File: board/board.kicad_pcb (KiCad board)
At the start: 2 copper layers, 195 x 160 mm, 234 parts, among them J1 Conn_02x03_Odd_Even, J3 RPi_GPIO, SW1 SW_Push, SW2 SW_Push, SW3 SW_Push, SW4 SW_Push, U1 74HC238, U10 A3144, U11 A3144, U12 A3144, U13 A3144, U14 A3144, U15 A3144, U16 A3144, U17 A3144, U18 A3144, U19 A3144, U2 74LS151, U20 A3144, U21 A3144, U22 A3144, U23 A3144, U24 A3144, U25 A3144, U26 A3144, U27 A3144, U28 A3144, U29 A3144, U3 A3144, U30 A3144, U31 A3144, U32 A3144, U33 A3144, U34 A3144, U35 A3144, U36 A3144, U37 A3144, U38 A3144, U39 A3144, U4 A3144, U40 A3144, U41 A3144, U42 A3144, U43 A3144, U44 A3144, U45 A3144, U46 A3144, U47 A3144, U48 A3144, U49 A3144, U5 A3144, U50 A3144, U51 A3144, U52 A3144, U53 A3144, U54 A3144, U55 A3144, U56 A3144, U57 A3144, U58 A3144, U59 A3144, U6 A3144, U60 A3144, U61 A3144, U62 A3144, U63 A3144, U64 A3144, U65 A3144, U66 A3144, U7 A3144, U8 A3144, U9 A3144

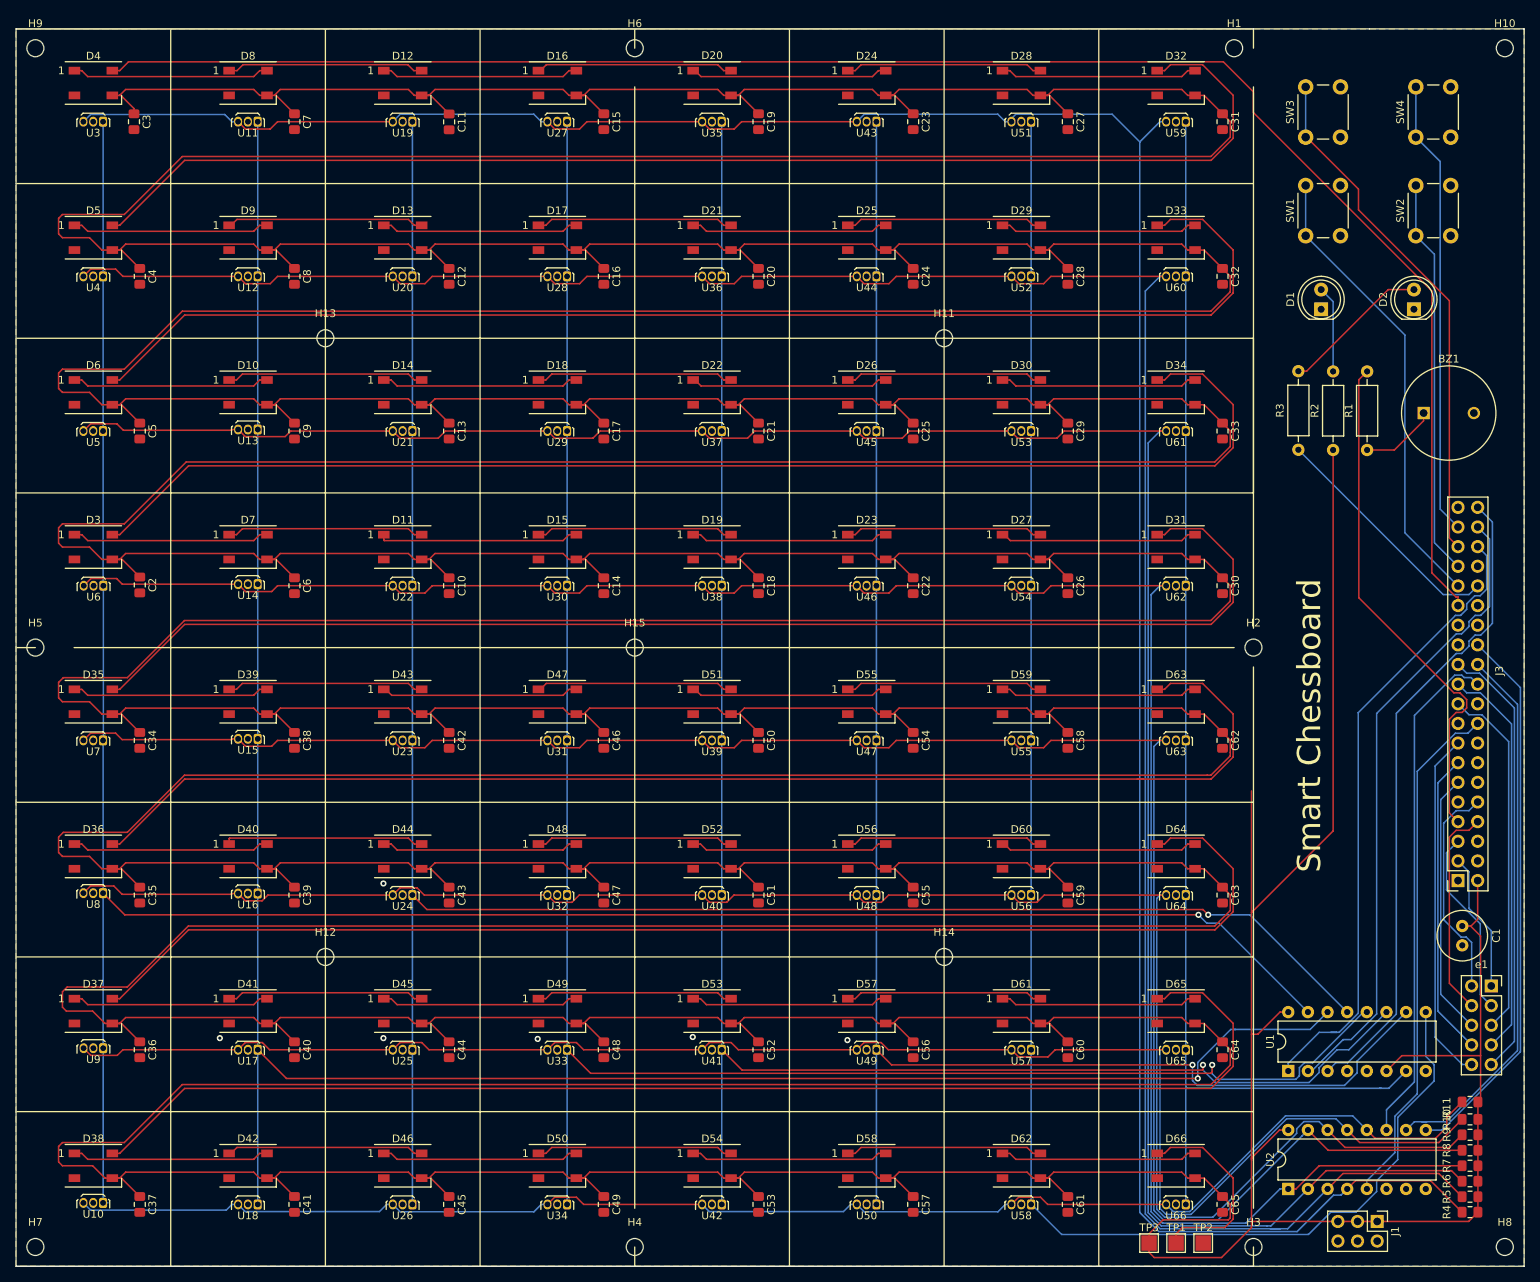
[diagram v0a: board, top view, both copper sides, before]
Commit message: Raspberry pi zero outline added
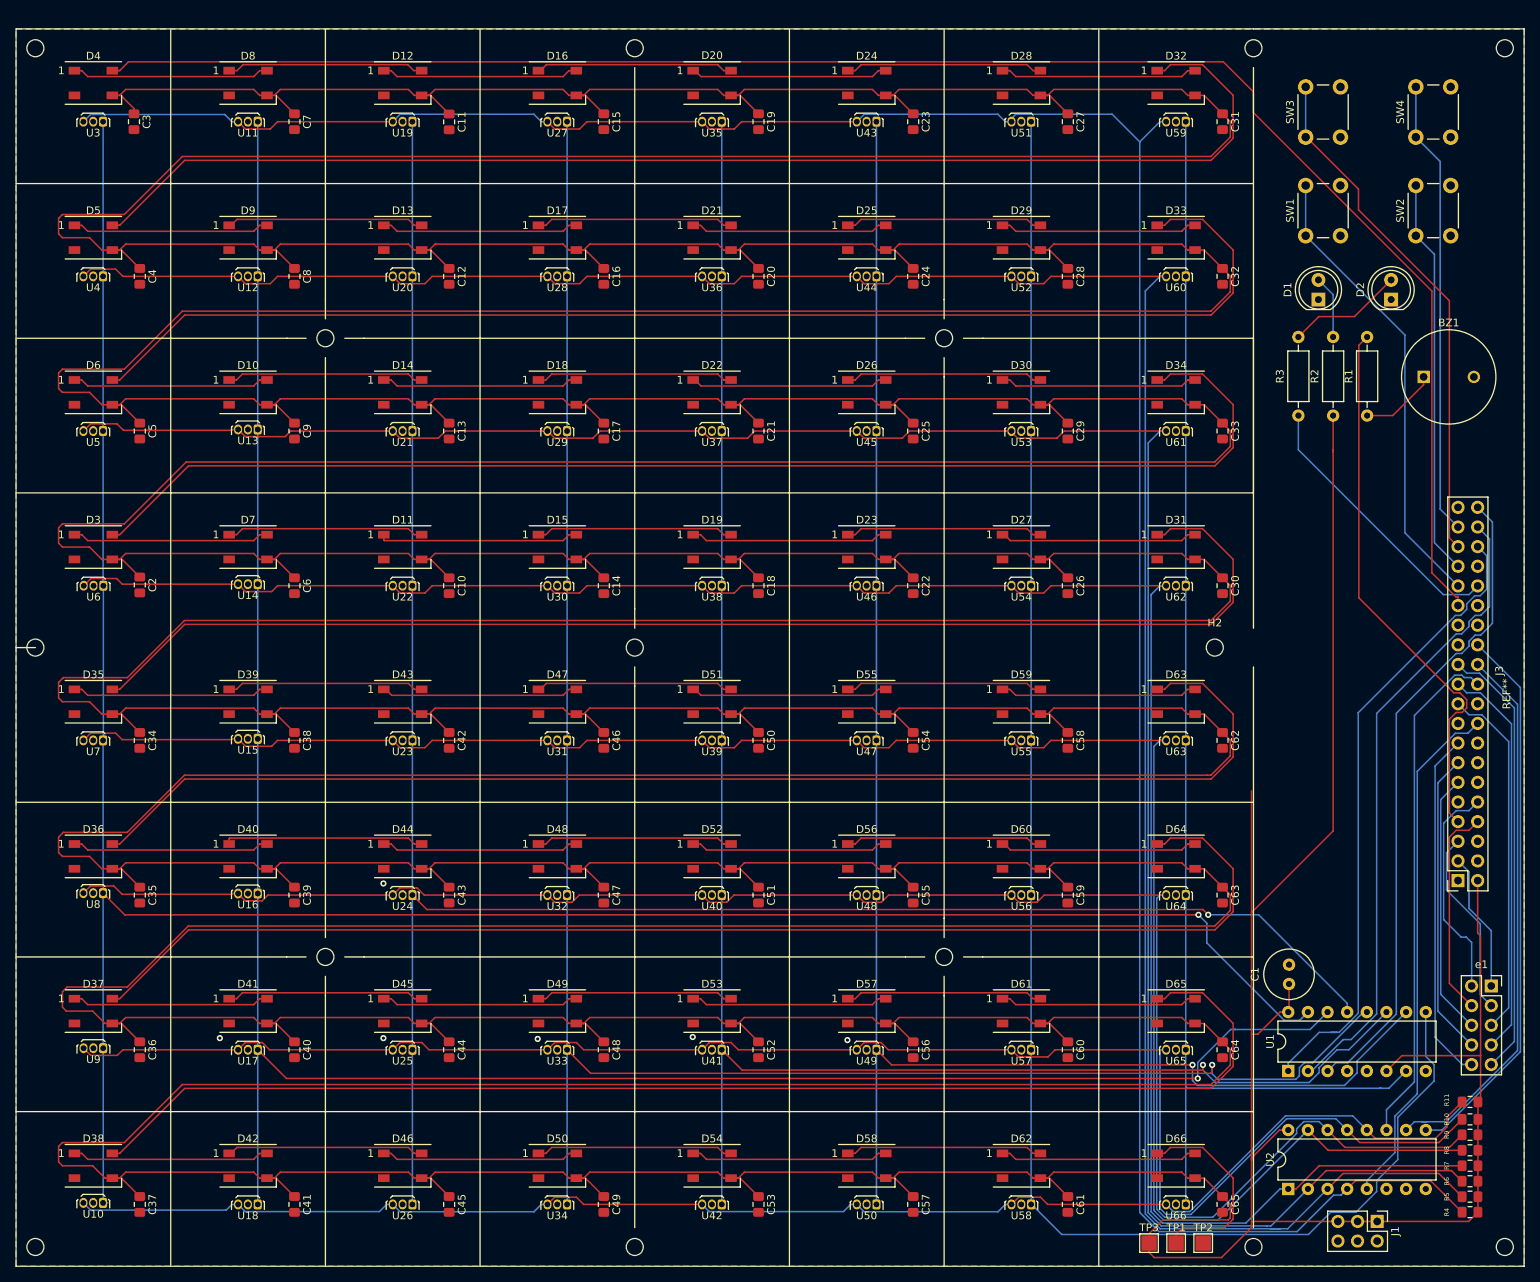
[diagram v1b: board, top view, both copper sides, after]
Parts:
- added REF**: rpi_zero_outline, board:rpi_zero_outline, F.Cu at (246.5, 160.1)
- moved C1 23.6 mm to (224.6, 173.5), turned to 90 degrees
- moved H2 5.00 mm to (215.0, 130.0)
- moved BZ1 4.67 mm to (242.0, 95.0)
- moved R1 4.45 mm to (234.7, 100.0)
- moved R2 4.45 mm to (230.3, 100.0)
- moved R3 4.42 mm to (225.8, 100.0)
- moved D2 3.20 mm to (237.8, 85.0)
- moved H1 2.50 mm to (220.0, 52.5)
- moved D1 1.30 mm to (228.4, 85.0)
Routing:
- net +5V: track 2879.4 -> 2885.9 mm
- net /BUZZER: track 66.7 -> 71.2 mm
- net /STAT_LED: track 31.4 -> 35.8 mm
- net Net-(D2-Pad2): track 19.3 -> 15.1 mm
- net Net-(D1-Pad2): track 11.2 -> 8.17 mm
- net D_0: track 302.6 -> 305.0 mm
- net D_2: track 267.1 -> 267.8 mm
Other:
- board text added: "Smart chessboard"
- board text removed: "Chessboard"
- board text removed: "Smart"
- board text removed: "Smart Chessboard"

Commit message: WS2812B test code added
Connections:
- J3 pad 1: (no net) -> Net-(J3-Pad1)
- J3 pad 12: (no net) -> LED_DATA
- J3 pad 14: (no net) -> Net-(J3-Pad14)
- J3 pad 16: (no net) -> Net-(J3-Pad16)
- J3 pad 17: (no net) -> Net-(J3-Pad17)
- J3 pad 20: (no net) -> Net-(J3-Pad20)
- J3 pad 25: (no net) -> Net-(J3-Pad25)
- J3 pad 27: (no net) -> Net-(J3-Pad27)
- J3 pad 28: (no net) -> Net-(J3-Pad28)
- J3 pad 29: LED_DATA -> Net-(J3-Pad29)
- J3 pad 30: (no net) -> Net-(J3-Pad30)
- J3 pad 34: (no net) -> Net-(J3-Pad34)
- J3 pad 4: (no net) -> Net-(J3-Pad4)
- J3 pad 6: (no net) -> Net-(J3-Pad6)
- J3 pad 9: (no net) -> Net-(J3-Pad9)
- U2 pad 6: (no net) -> Net-(U2-Pad6)
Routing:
- net LED_DATA: track 227.2 -> 254.5 mm
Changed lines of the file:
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@@
   (general
     (thickness 1.6)
-    (drawings 110)
-    (tracks 1612)
+    (drawings 114)
+    (tracks 1613)
     (zones 0)
     (modules 235)
-    (nets 110)
+    (nets 125)
   )
   (page A3)
@@
   (net 108 /AUX7)
   (net 109 /BTN4)
+  (net 110 "Net-(J3-Pad30)")
+  (net 111 "Net-(J3-Pad20)")
+  (net 112 "Net-(J3-Pad6)")
+  (net 113 "Net-(J3-Pad34)")
+  (net 114 "Net-(J3-Pad1)")
+  (net 115 "Net-(J3-Pad4)")
+  (net 116 "Net-(J3-Pad28)")
+  (net 117 "Net-(J3-Pad29)")
+  (net 118 "Net-(J3-Pad9)")
+  (net 119 "Net-(J3-Pad27)")
+  (net 120 "Net-(J3-Pad14)")
+  (net 121 "Net-(J3-Pad17)")
+  (net 122 "Net-(J3-Pad25)")
+  (net 123 "Net-(J3-Pad16)")
+  (net 124 "Net-(U2-Pad6)")
   (net_class Default "This is the default net class."
     (clearance 0.17)
@@
     (add_net "Net-(D62-Pad1)")
     (add_net "Net-(D66-Pad1)")
+    (add_net "Net-(J3-Pad1)")
+    (add_net "Net-(J3-Pad14)")
+    (add_net "Net-(J3-Pad16)")
+    (add_net "Net-(J3-Pad17)")
+    (add_net "Net-(J3-Pad20)")
+    (add_net "Net-(J3-Pad25)")
+    (add_net "Net-(J3-Pad27)")
+    (add_net "Net-(J3-Pad28)")
+    (add_net "Net-(J3-Pad29)")
+    (add_net "Net-(J3-Pad30)")
+    (add_net "Net-(J3-Pad34)")
+    (add_net "Net-(J3-Pad4)")
+    (add_net "Net-(J3-Pad6)")
+    (add_net "Net-(J3-Pad9)")
+    (add_net "Net-(U2-Pad6)")
   )
   (net_class Power ""
@@
     (pad 13 thru_hole oval (at -1.55 11.885 180) (size 1.7 1.7) (drill 1) (layers *.Cu *.Mask)
       (net 106 /AUX9))
-    (pad 30 thru_hole oval (at 0.99 -8.435 180) (size 1.7 1.7) (drill 1) (layers *.Cu *.Mask))
-    (pad 20 thru_hole oval (at 0.99 4.265 180) (size 1.7 1.7) (drill 1) (layers *.Cu *.Mask))
+    (pad 30 thru_hole oval (at 0.99 -8.435 180) (size 1.7 1.7) (drill 1) (layers *.Cu *.Mask)
+      (net 110 "Net-(J3-Pad30)"))
+    (pad 20 thru_hole oval (at 0.99 4.265 180) (size 1.7 1.7) (drill 1) (layers *.Cu *.Mask)
+      (net 111 "Net-(J3-Pad20)"))
     (pad 11 thru_hole oval (at -1.55 14.425 180) (size 1.7 1.7) (drill 1) (layers *.Cu *.Mask)
       (net 107 /AUX8))
-    (pad 6 thru_hole oval (at 0.99 22.045 180) (size 1.7 1.7) (drill 1) (layers *.Cu *.Mask))
+    (pad 6 thru_hole oval (at 0.99 22.045 180) (size 1.7 1.7) (drill 1) (layers *.Cu *.Mask)
+      (net 112 "Net-(J3-Pad6)"))
     (pad 8 thru_hole oval (at 0.99 19.505 180) (size 1.7 1.7) (drill 1) (layers *.Cu *.Mask)
       (net 108 /AUX7))
@@
     (pad 7 thru_hole oval (at -1.55 19.505 180) (size 1.7 1.7) (drill 1) (layers *.Cu *.Mask)
       (net 16 /BUZZER))
-    (pad 34 thru_hole oval (at 0.99 -13.515 180) (size 1.7 1.7) (drill 1) (layers *.Cu *.Mask))
+    (pad 34 thru_hole oval (at 0.99 -13.515 180) (size 1.7 1.7) (drill 1) (layers *.Cu *.Mask)
+      (net 113 "Net-(J3-Pad34)"))
     (pad 35 thru_hole oval (at -1.55 -16.055 180) (size 1.7 1.7) (drill 1) (layers *.Cu *.Mask)
       (net 7 /BTN3))
@@
     (pad 38 thru_hole oval (at 0.99 -18.595 180) (size 1.7 1.7) (drill 1) (layers *.Cu *.Mask)
       (net 13 D_S1))
-    (pad 1 thru_hole rect (at -1.55 27.125 180) (size 1.7 1.7) (drill 1) (layers *.Cu *.Mask))
-    (pad 4 thru_hole oval (at 0.99 24.585 180) (size 1.7 1.7) (drill 1) (layers *.Cu *.Mask))
+    (pad 1 thru_hole rect (at -1.55 27.125 180) (size 1.7 1.7) (drill 1) (layers *.Cu *.Mask)
+      (net 114 "Net-(J3-Pad1)"))
+    (pad 4 thru_hole oval (at 0.99 24.585 180) (size 1.7 1.7) (drill 1) (layers *.Cu *.Mask)
+      (net 115 "Net-(J3-Pad4)"))
     (pad 24 thru_hole oval (at 0.99 -0.815 180) (size 1.7 1.7) (drill 1) (layers *.Cu *.Mask)
       (net 9 M_S1))
     (pad 18 thru_hole oval (at 0.99 6.805 180) (size 1.7 1.7) (drill 1) (layers *.Cu *.Mask)
       (net 10 MUX_OUT))
-    (pad 28 thru_hole oval (at 0.99 -5.895 180) (size 1.7 1.7) (drill 1) (layers *.Cu *.Mask))
+    (pad 28 thru_hole oval (at 0.99 -5.895 180) (size 1.7 1.7) (drill 1) (layers *.Cu *.Mask)
+      (net 116 "Net-(J3-Pad28)"))
     (pad 29 thru_hole oval (at -1.55 -8.435 180) (size 1.7 1.7) (drill 1) (layers *.Cu *.Mask)
-      (net 27 LED_DATA))
-    (pad 9 thru_hole oval (at -1.55 16.965 180) (size 1.7 1.7) (drill 1) (layers *.Cu *.Mask))
+      (net 117 "Net-(J3-Pad29)"))
+    (pad 9 thru_hole oval (at -1.55 16.965 180) (size 1.7 1.7) (drill 1) (layers *.Cu *.Mask)
+      (net 118 "Net-(J3-Pad9)"))
     (pad 19 thru_hole oval (at -1.55 4.265 180) (size 1.7 1.7) (drill 1) (layers *.Cu *.Mask)
       (net 19 /AUX3))
@@
     (pad 21 thru_hole oval (at -1.55 1.725 180) (size 1.7 1.7) (drill 1) (layers *.Cu *.Mask)
       (net 18 /AUX4))
-    (pad 27 thru_hole oval (at -1.55 -5.895 180) (size 1.7 1.7) (drill 1) (layers *.Cu *.Mask))
-    (pad 14 thru_hole oval (at 0.99 11.885 180) (size 1.7 1.7) (drill 1) (layers *.Cu *.Mask))
+    (pad 27 thru_hole oval (at -1.55 -5.895 180) (size 1.7 1.7) (drill 1) (layers *.Cu *.Mask)
+      (net 119 "Net-(J3-Pad27)"))
+    (pad 14 thru_hole oval (at 0.99 11.885 180) (size 1.7 1.7) (drill 1) (layers *.Cu *.Mask)
+      (net 120 "Net-(J3-Pad14)"))
     (pad 32 thru_hole oval (at 0.99 -10.975 180) (size 1.7 1.7) (drill 1) (layers *.Cu *.Mask)
       (net 11 /STAT_LED))
-    (pad 17 thru_hole oval (at -1.55 6.805 180) (size 1.7 1.7) (drill 1) (layers *.Cu *.Mask))
-    (pad 12 thru_hole oval (at 0.99 14.425 180) (size 1.7 1.7) (drill 1) (layers *.Cu *.Mask))
+    (pad 17 thru_hole oval (at -1.55 6.805 180) (size 1.7 1.7) (drill 1) (layers *.Cu *.Mask)
+      (net 121 "Net-(J3-Pad17)"))
+    (pad 12 thru_hole oval (at 0.99 14.425 180) (size 1.7 1.7) (drill 1) (layers *.Cu *.Mask)
+      (net 27 LED_DATA))
     (pad 26 thru_hole oval (at 0.99 -3.355 180) (size 1.7 1.7) (drill 1) (layers *.Cu *.Mask)
       (net 14 M_S2))
-    (pad 25 thru_hole oval (at -1.55 -3.355 180) (size 1.7 1.7) (drill 1) (layers *.Cu *.Mask))
+    (pad 25 thru_hole oval (at -1.55 -3.355 180) (size 1.7 1.7) (drill 1) (layers *.Cu *.Mask)
+      (net 122 "Net-(J3-Pad25)"))
     (pad 37 thru_hole oval (at -1.55 -18.595 180) (size 1.7 1.7) (drill 1) (layers *.Cu *.Mask)
       (net 109 /BTN4))
     (pad 23 thru_hole oval (at -1.55 -0.815 180) (size 1.7 1.7) (drill 1) (layers *.Cu *.Mask)
       (net 20 /AUX5))
-    (pad 16 thru_hole oval (at 0.99 9.345 180) (size 1.7 1.7) (drill 1) (layers *.Cu *.Mask))
+    (pad 16 thru_hole oval (at 0.99 9.345 180) (size 1.7 1.7) (drill 1) (layers *.Cu *.Mask)
+      (net 123 "Net-(J3-Pad16)"))
     (pad 2 thru_hole oval (at 0.99 27.125 180) (size 1.7 1.7) (drill 1) (layers *.Cu *.Mask)
       (net 2 +5V))
@@
     (pad 13 thru_hole oval (at 7.62 7.62 90) (size 1.6 1.6) (drill 0.8) (layers *.Cu *.Mask)
       (net 95 M_6))
-    (pad 6 thru_hole oval (at 0 12.7 90) (size 1.6 1.6) (drill 0.8) (layers *.Cu *.Mask))
+    (pad 6 thru_hole oval (at 0 12.7 90) (size 1.6 1.6) (drill 0.8) (layers *.Cu *.Mask)
+      (net 124 "Net-(U2-Pad6)"))
     (pad 14 thru_hole oval (at 7.62 5.08 90) (size 1.6 1.6) (drill 0.8) (layers *.Cu *.Mask)
       (net 94 M_5))
@@
     )
   )
+  (gr_line (start 137 130) (end 66 130) (layer F.SilkS) (width 0.15))
+  (gr_line (start 213 130) (end 143 130) (layer F.SilkS) (width 0.15))
+  (gr_line (start 217 130) (end 220 130) (layer F.SilkS) (width 0.15))
+  (gr_line (start 220 127.5) (end 220 132.5) (layer F.SilkS) (width 0.15))
   (dimension 195 (width 0.15) (layer Dwgs.User)
     (gr_text "195.000 mm" (at 157.5 25.7) (layer Dwgs.User)
@@
   (segment (start 90.73 56.17) (end 91.5 55.4) (width 0.2) (layer F.Cu) (net 26))
   (segment (start 91.5 55.4) (end 92.45 55.4) (width 0.2) (layer F.Cu) (net 26))
-  (segment (start 246.45 124.565) (end 246.45 123.4447) (width 0.2) (layer F.Cu) (net 27))
-  (segment (start 219.9979 60.8268) (end 243.0703 83.8992) (width 0.2) (layer F.Cu) (net 27))
-  (segment (start 243.0703 83.8992) (end 243.0703 120.3369) (width 0.2) (layer F.Cu) (net 27))
-  (segment (start 243.0703 120.3369) (end 246.1781 123.4447) (width 0.2) (layer F.Cu) (net 27))
-  (segment (start 246.1781 123.4447) (end 246.45 123.4447) (width 0.2) (layer F.Cu) (net 27))
+  (segment (start 251 145.415) (end 248.99 147.425) (width 0.2) (layer F.Cu) (net 27))
+  (segment (start 251 124.917398) (end 251 145.415) (width 0.2) (layer F.Cu) (net 27))
+  (segment (start 249.227603 123.145001) (end 251 124.917398) (width 0.2) (layer F.Cu) (net 27))
+  (segment (start 243.0703 120.3369) (end 245.878401 123.145001) (width 0.2) (layer F.Cu) (net 27))
+  (segment (start 73.4 55.4) (end 74.54031 54.25969) (width 0.2) (layer F.Cu) (net 27))
+  (segment (start 245.878401 123.145001) (end 249.227603 123.145001) (width 0.2) (layer F.Cu) (net 27))
   (segment (start 72.45 55.4) (end 73.4 55.4) (width 0.2) (layer F.Cu) (net 27))
-  (segment (start 219.9979 60.8268) (end 219.9979 58.1479) (width 0.2) (layer F.Cu) (net 27))
-  (segment (start 74.54031 54.25969) (end 74.475 54.325) (width 0.2) (layer F.Cu) (net 27))
-  (segment (start 216.10969 54.25969) (end 74.54031 54.25969) (width 0.2) (layer F.Cu) (net 27))
-  (segment (start 219.9979 58.1479) (end 216.10969 54.25969) (width 0.2) (layer F.Cu) (net 27))
-  (segment (start 73.4 55.4) (end 74.475 54.325) (width 0.2) (layer F.Cu) (net 27))
+  (segment (start 74.54031 54.25969) (end 216.10969 54.25969) (width 0.2) (layer F.Cu) (net 27))
+  (segment (start 243.0703 83.8992) (end 243.0703 120.3369) (width 0.2) (layer F.Cu) (net 27))
+  (segment (start 216.10969 54.25969) (end 219.9979 58.1479) (width 0.2) (layer F.Cu) (net 27))
+  (segment (start 219.9979 58.1479) (end 219.9979 60.8268) (width 0.2) (layer F.Cu) (net 27))
+  (segment (start 219.9979 60.8268) (end 243.0703 83.8992) (width 0.2) (layer F.Cu) (net 27))
   (segment (start 67.55 75.4) (end 68.5 75.4) (width 0.2) (layer F.Cu) (net 28))
   (segment (start 68.5 75.4) (end 69.27 76.17) (width 0.2) (layer F.Cu) (net 28))
